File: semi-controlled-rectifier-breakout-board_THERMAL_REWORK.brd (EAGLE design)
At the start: 152.4 x 101.6 mm, 18 parts, among them U10 VO3053-X007T, U11 VO3053-X007T, U8 TN4015H-6G, U9 TN4015H-6G, X1 22-23-2031

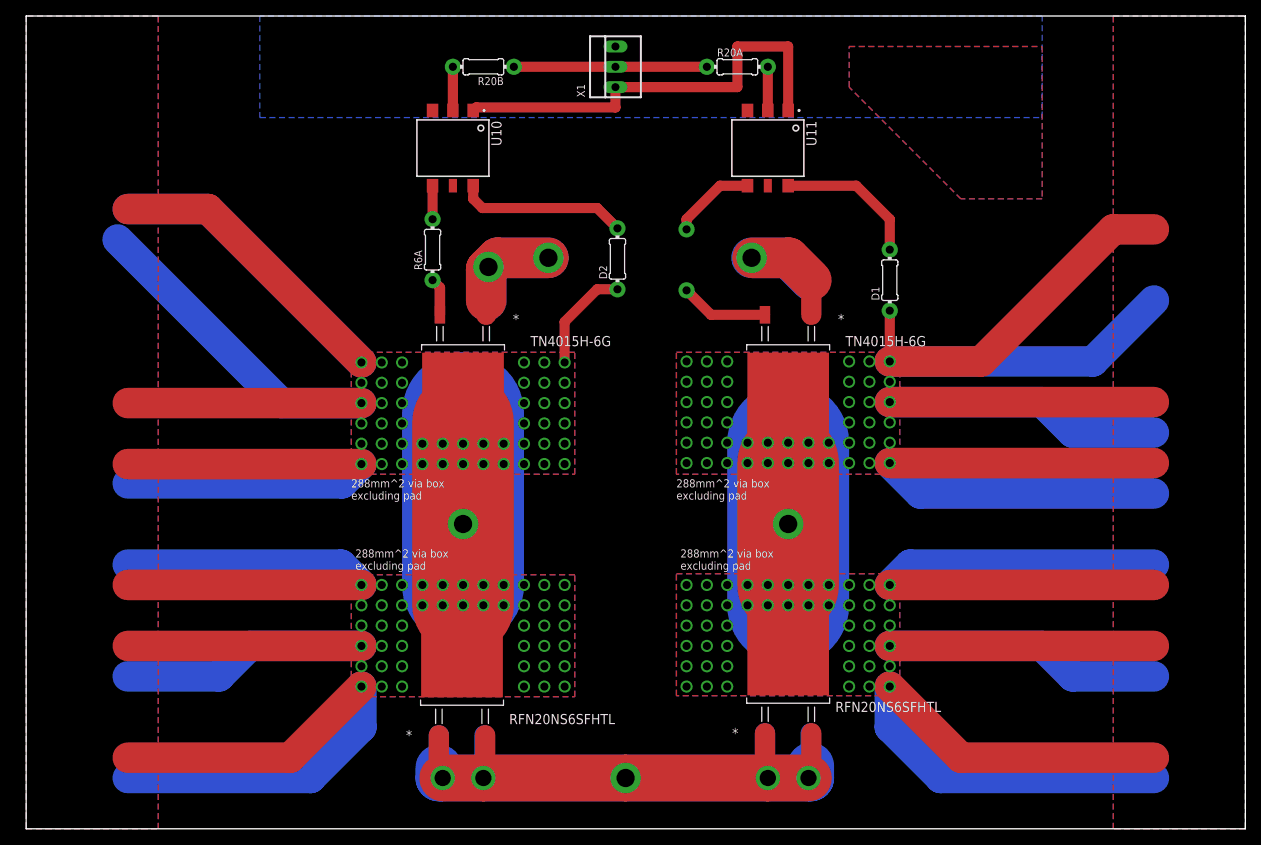
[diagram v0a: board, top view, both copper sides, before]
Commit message: Generated flatcam files for 2 sided pcb with thermal vias. Exported as gcode
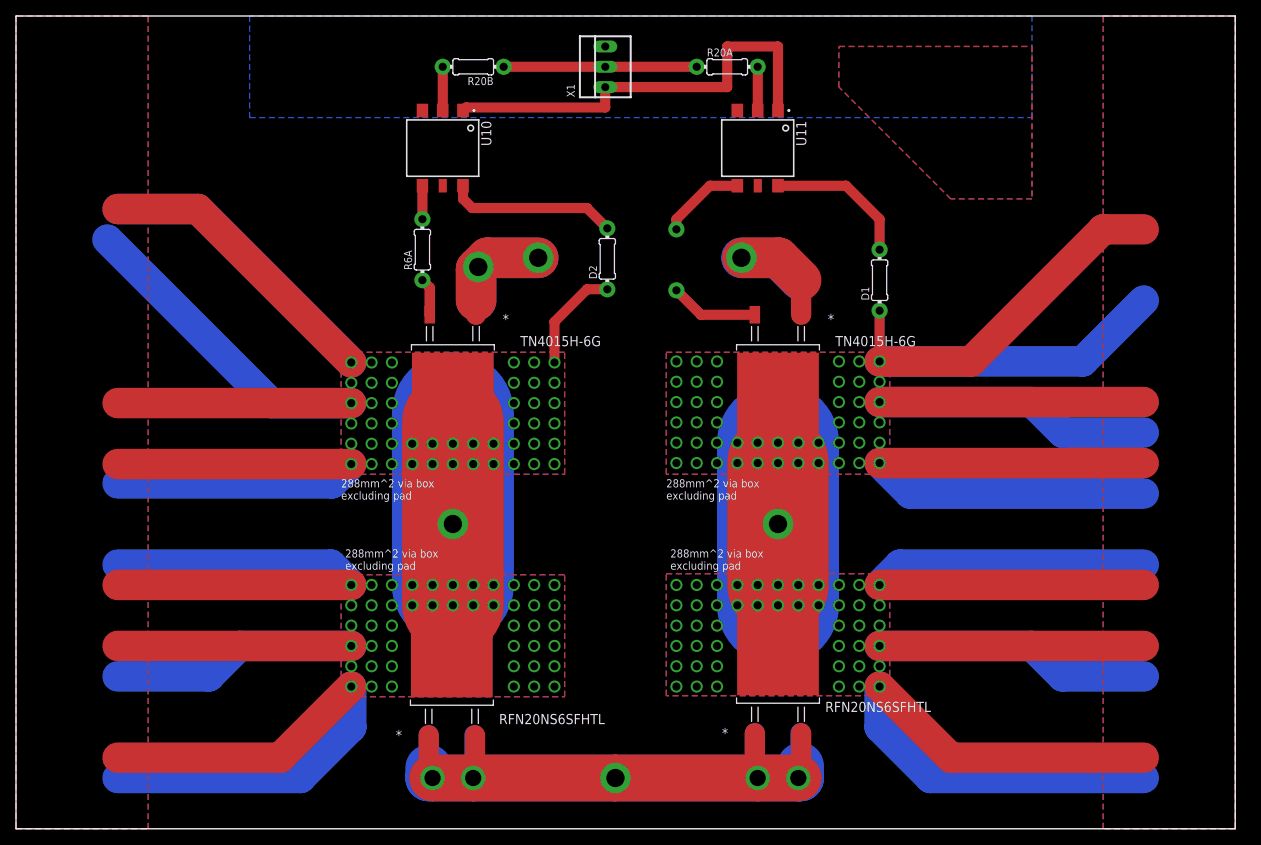
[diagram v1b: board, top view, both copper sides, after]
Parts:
- moved D1 1.27 mm to (96.5, 68.6)
- moved D9 1.27 mm to (83.8, 20.3)
- moved U$2 1.27 mm to (83.8, 38.1)
- moved U9 1.27 mm to (83.8, 55.9)
- moved D8 1.27 mm to (43.1, 20.1)
- moved R20B 1.27 mm to (45.7, 95.2)
- moved R6A 1.27 mm to (39.4, 72.4)
- moved U$1 1.27 mm to (43.2, 38.1)
- moved U$3 1.27 mm to (46.4, 70.2)
- moved U10 1.27 mm to (41.9, 85.1)
- moved U8 1.27 mm to (43.2, 55.9)
- moved X1 1.27 mm to (62.2, 95.2)
- moved D2 1.27 mm to (62.5, 71.2)
- moved R20A 1.27 mm to (77.5, 95.2)
- moved R6B 1.27 mm to (71.1, 71.1)
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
